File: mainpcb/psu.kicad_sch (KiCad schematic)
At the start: 15 parts, among them U1 LM22678TJ-5, U2 LM2576T-3.3

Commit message: Added PSU terminal block symbol
Also created bh_part_library for custom modelled parts used in the bot-hoven project.
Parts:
- added J1: 8PCV-06-006, symbol bh_part_library:8PCV-06-006
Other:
- note added: "SCREW TERMINALS TO MEANWELL LRS-XXX-24 POWER SUPPLY XXX - POWER RATING NOT YET SPECIFIED (200-350W)"
- moved on the sheet: C1, C2, C3, C4, C5, C6, C7, C8, C9, D1, D2, L1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

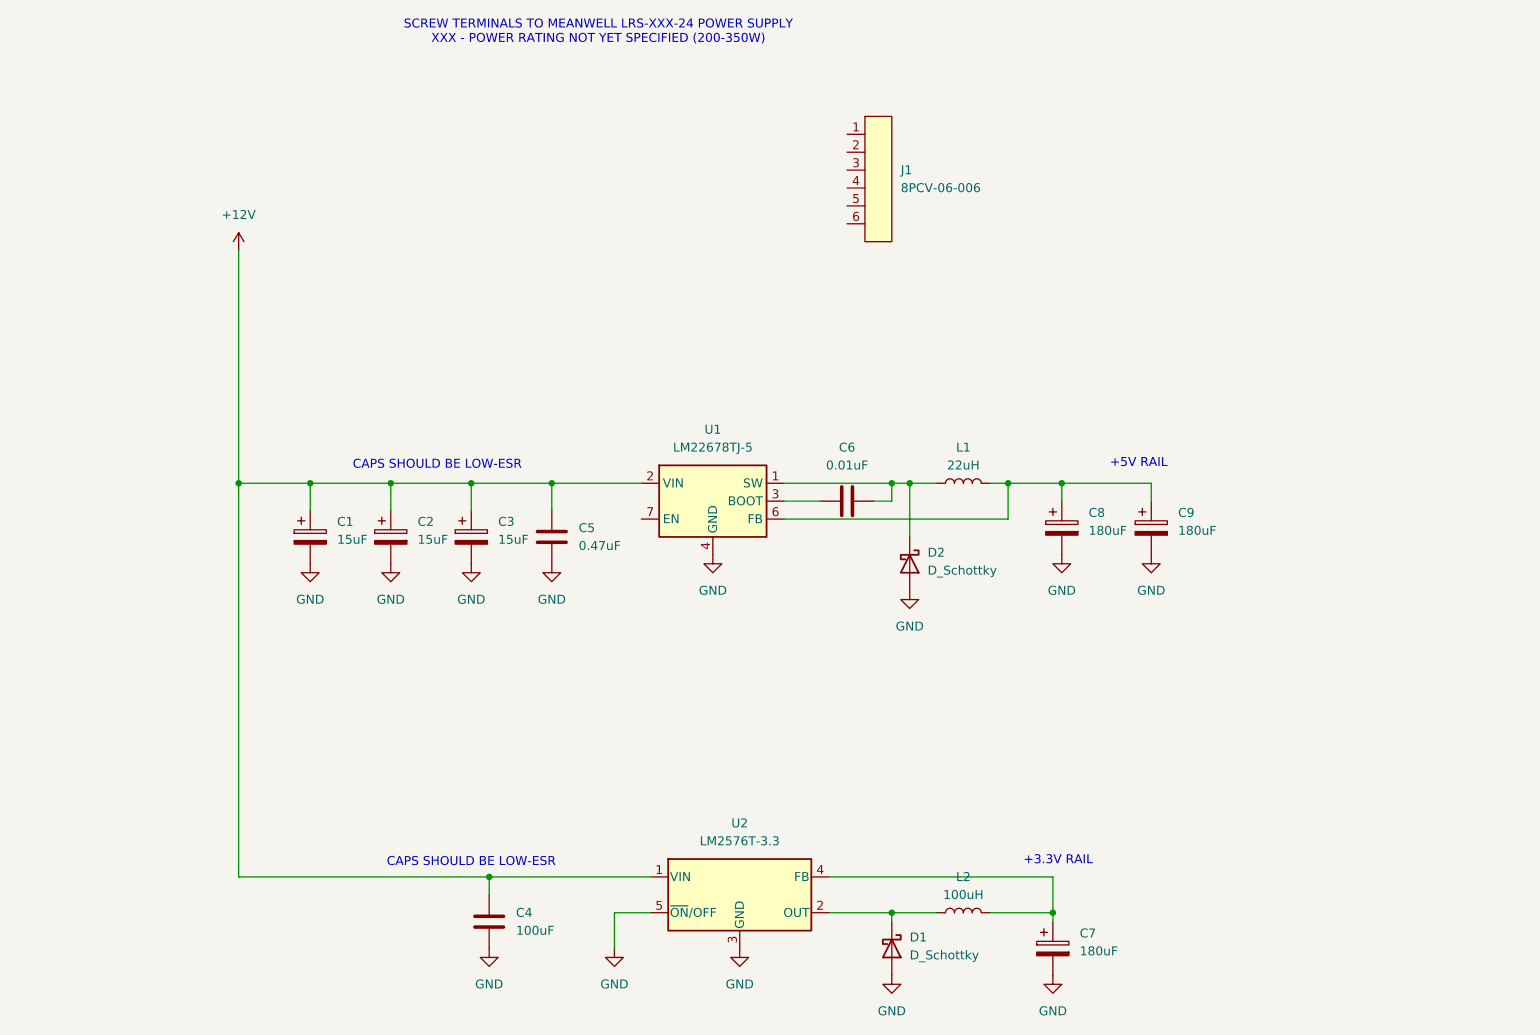
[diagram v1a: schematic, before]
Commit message: Some hand components, PSU changes
Updated PSU to 24V rail regulated to 5V and 3.3V. Hopefully we won't need a 12V rail. Made some part selections, added IO expander for hand, mosfet, made solenoid symbol.
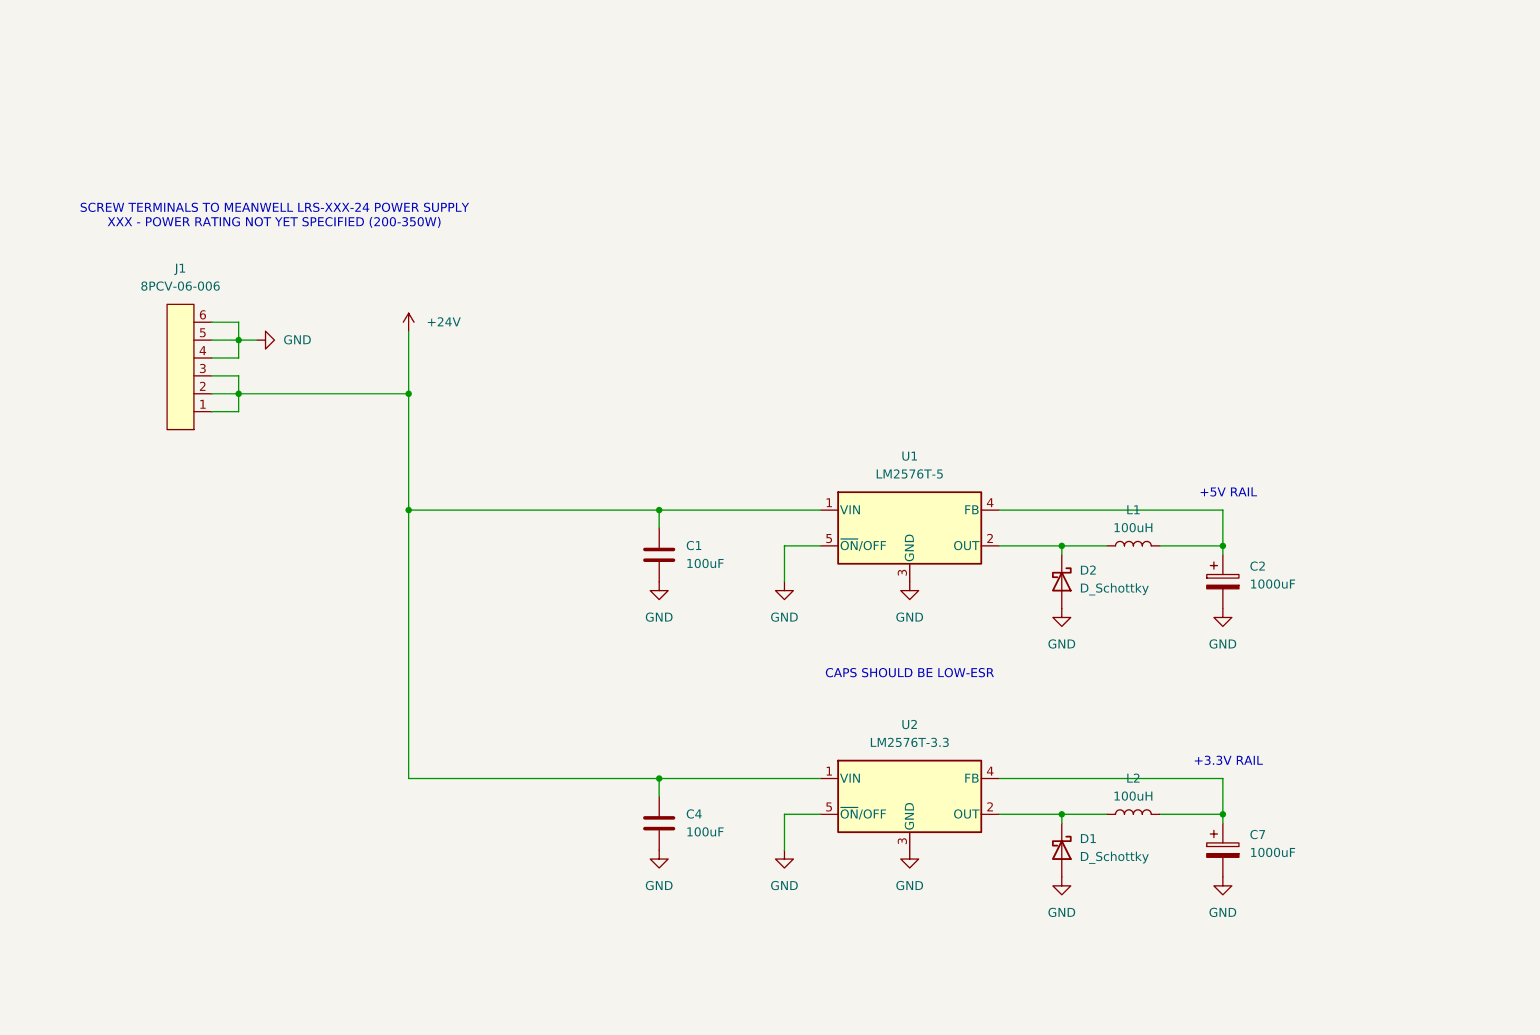
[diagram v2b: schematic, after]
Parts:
- removed C1, C3: 15uF, symbol Device:C_Polarized
- removed C5: 0.47uF, symbol Device:C
- removed C6: 0.01uF, symbol Device:C
- removed C8, C9: 180uF, symbol Device:C_Polarized
- removed J1: 8PCV-06-006, symbol bh_part_library:8PCV-06-006
- removed U1: LM22678TJ-5, Package_TO_SOT_THT:TO-220-7_P2.54x3.7mm_StaggerOdd_Lead3.8mm_Vertical, symbol Regulator_Switching:LM22678TJ-5
- added C1: 100uF, symbol Device:C
- added J1: 8PCV-06-006, symbol bh_symbol_library:8PCV-06-006
- added U1: LM2576T-5, Package_TO_SOT_THT:TO-220-5_Vertical, symbol Regulator_Switching:LM2576T-5
- C2: value 15uF -> 1000uF
- C7: value 180uF -> 1000uF
- L1: value 22uH -> 100uH
- U2: footprint Package_TO_SOT_THT:TO-220-5_Vertical -> Package_TO_SOT_THT:TO-220-5_P3.4x3.7mm_StaggerOdd_Lead3.8mm_Vertical; Digikey (none) -> https://www.digikey.ca/en/products/detail/texas-instruments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
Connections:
- net GND: now also C1.2, J1.4, J1.5, J1.6, U1.3 (GND), U1.5 (~{ON}/OFF)
- net at D2.1 (K), L1.1: now also U1.2 (OUT)
- net at L1.2: now also C2.1, U1.4 (FB)
- net +12V renamed +24V
- net +24V: now also C1.1, J1.1, J1.2, J1.3, U1.1 (VIN); no longer C2.1
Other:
- moved on the sheet: C4, C7, D1, L2, U2

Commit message: Added 12V power rail and regulator
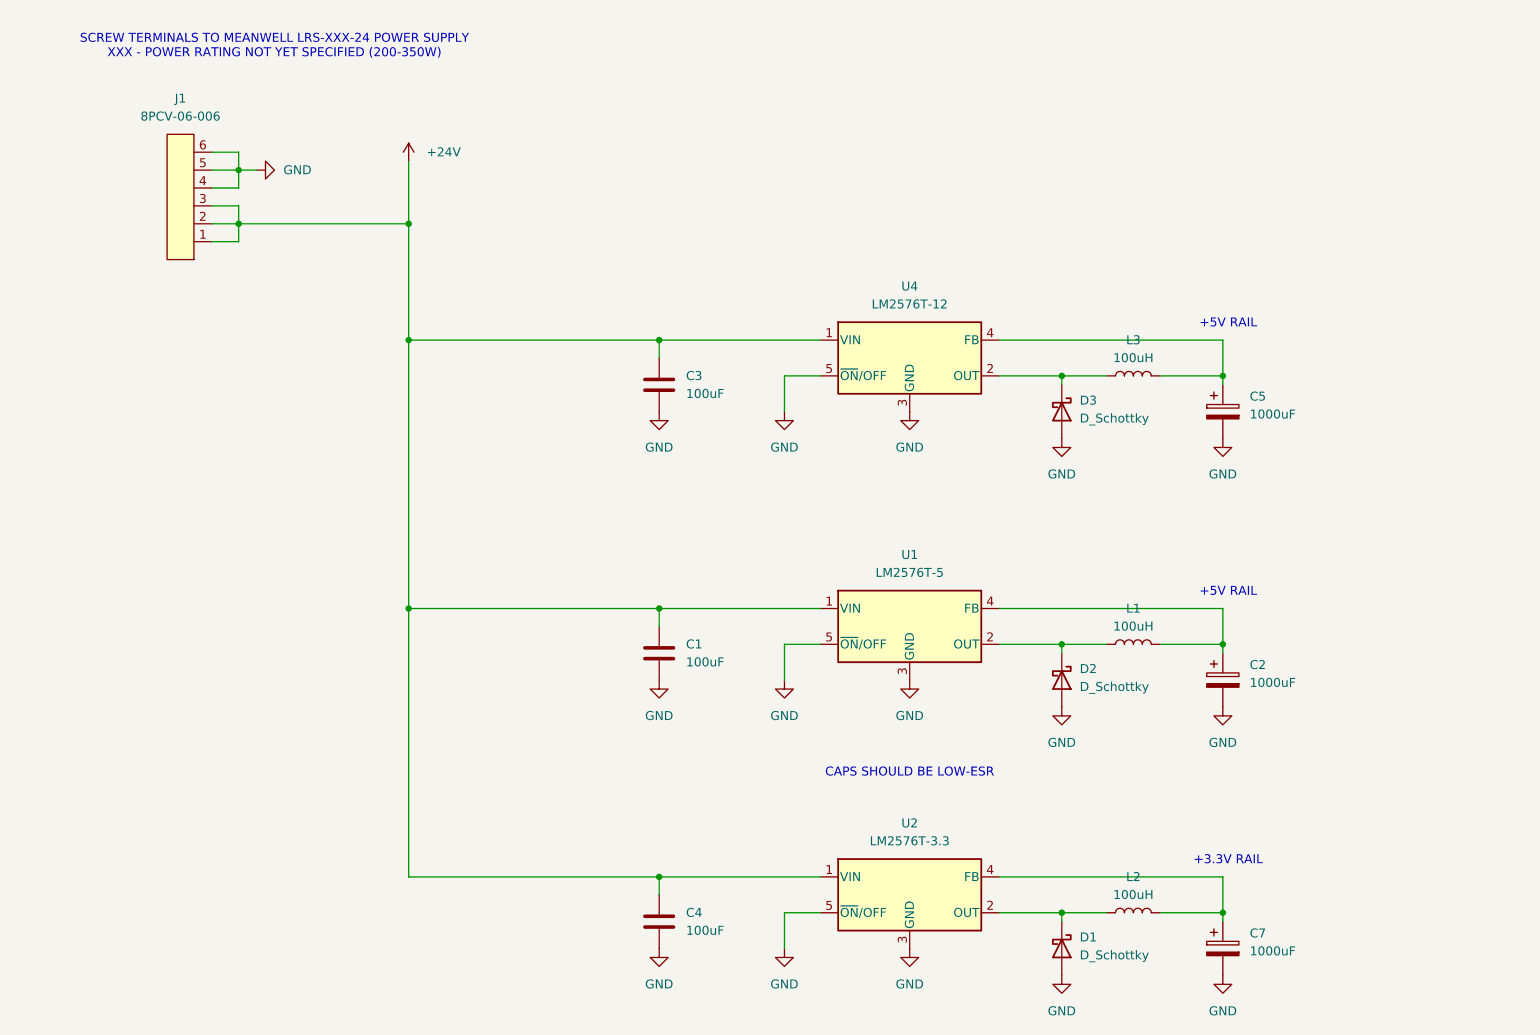
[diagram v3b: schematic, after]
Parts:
- added C3: 100uF, symbol Device:C
- added C5: 1000uF, symbol Device:C_Polarized
- added D3: D_Schottky, symbol Device:D_Schottky
- added L3: 100uH, symbol Device:L
- added U4: LM2576T-12, Package_TO_SOT_THT:TO-220-5_Vertical, symbol Regulator_Switching:LM2576T-12
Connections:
- net +24V: now also C3.1, U4.1 (VIN)
- net GND: now also C3.2, C5.2, D3.2 (A), U4.3 (GND), U4.5 (~{ON}/OFF)
- new net: D3.1 (K), L3.1, U4.2 (OUT)
- new net: C5.1, L3.2, U4.4 (FB)
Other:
- moved on the sheet: C1, C2, C4, C7, D1, D2, J1, L1, L2, U1, U2

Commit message: Created LM2678 12V regulator symbol
Updated 12V regulator circuit
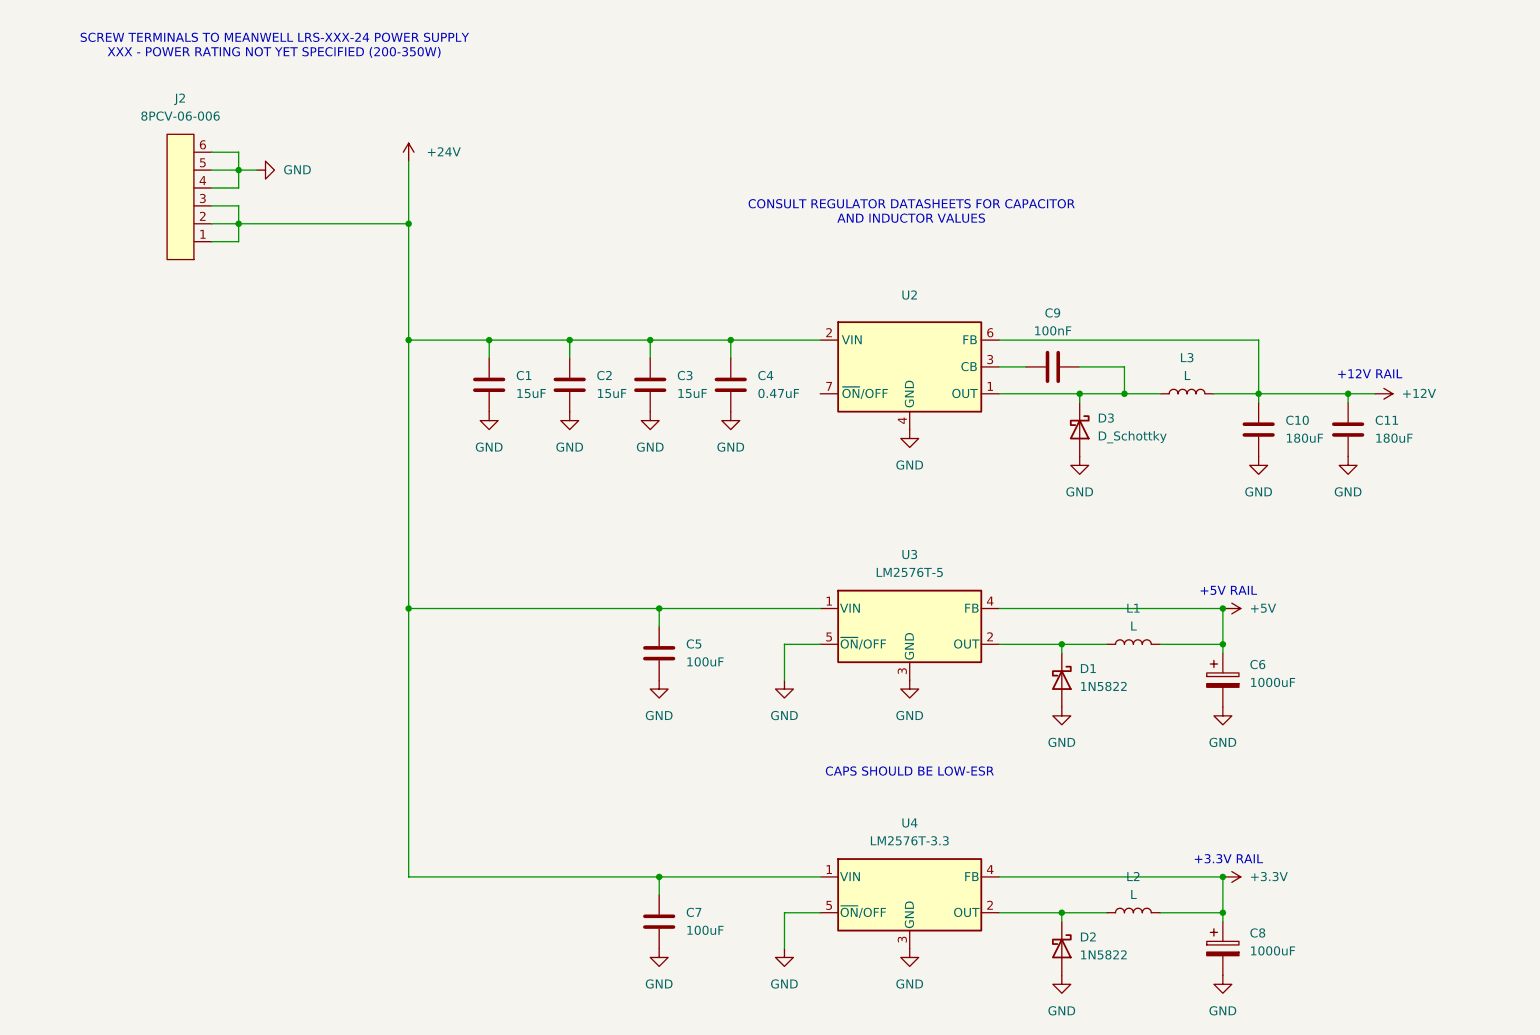
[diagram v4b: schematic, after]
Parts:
- removed C5: 1000uF, symbol Device:C_Polarized
- removed U4: LM2576T-12, Package_TO_SOT_THT:TO-220-5_Vertical, symbol Regulator_Switching:LM2576T-12
- added C1, C2: 15uF, symbol Device:C
- added C10, C11: 180uF, symbol Device:C
- added C4: 0.47uF, symbol Device:C
- added C9: 100nF, symbol Device:C
- added U2: ~, symbol bh_symbol_library:LM2678T-12
- C3: value 100uF -> 15uF
- D1: renamed from D2; value D_Schottky -> 1N5822
- D2: renamed from D1; value D_Schottky -> 1N5822
- D3: footprint (none) -> Package_TO_SOT_SMD:TO-263-2
- L1, L2, L3: value 100uH -> L
- renumbered C1 to C5, C2 to C6, C4 to C7, C7 to C8, J1 to J2, U1 to U3, U2 to U4
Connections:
- net +24V: now also C1.1, C2.1, C4.1, U2.2 (VIN)
- net GND: now also C1.2, C10.2, C11.2, C2.2, C4.2, U2.4 (GND)
- net at D3.1 (K), L3.1: now also C9.2, U2.1 (OUT)
- net +12V: now reaches L3.2
- net +12V: now also C10.1, C11.1, U2.6 (FB)
- net +3.3V: now reaches C8.1, L2.2, U4.4 (FB)
- net +5V: now reaches C6.1, L1.2, U3.4 (FB)
- new net: C9.1, U2.3 (CB)
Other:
- note added: "+12V RAIL"
- note added: "CONSULT REGULATOR DATASHEETS FOR CAPACITOR AND INDUCTOR VALUES"

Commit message: I2C transceivers, sheet hierarchy changes
Added I2C transceivers for both hands on the controller side, also changed sheet hierarchy to modularize controller board sheet somewhat
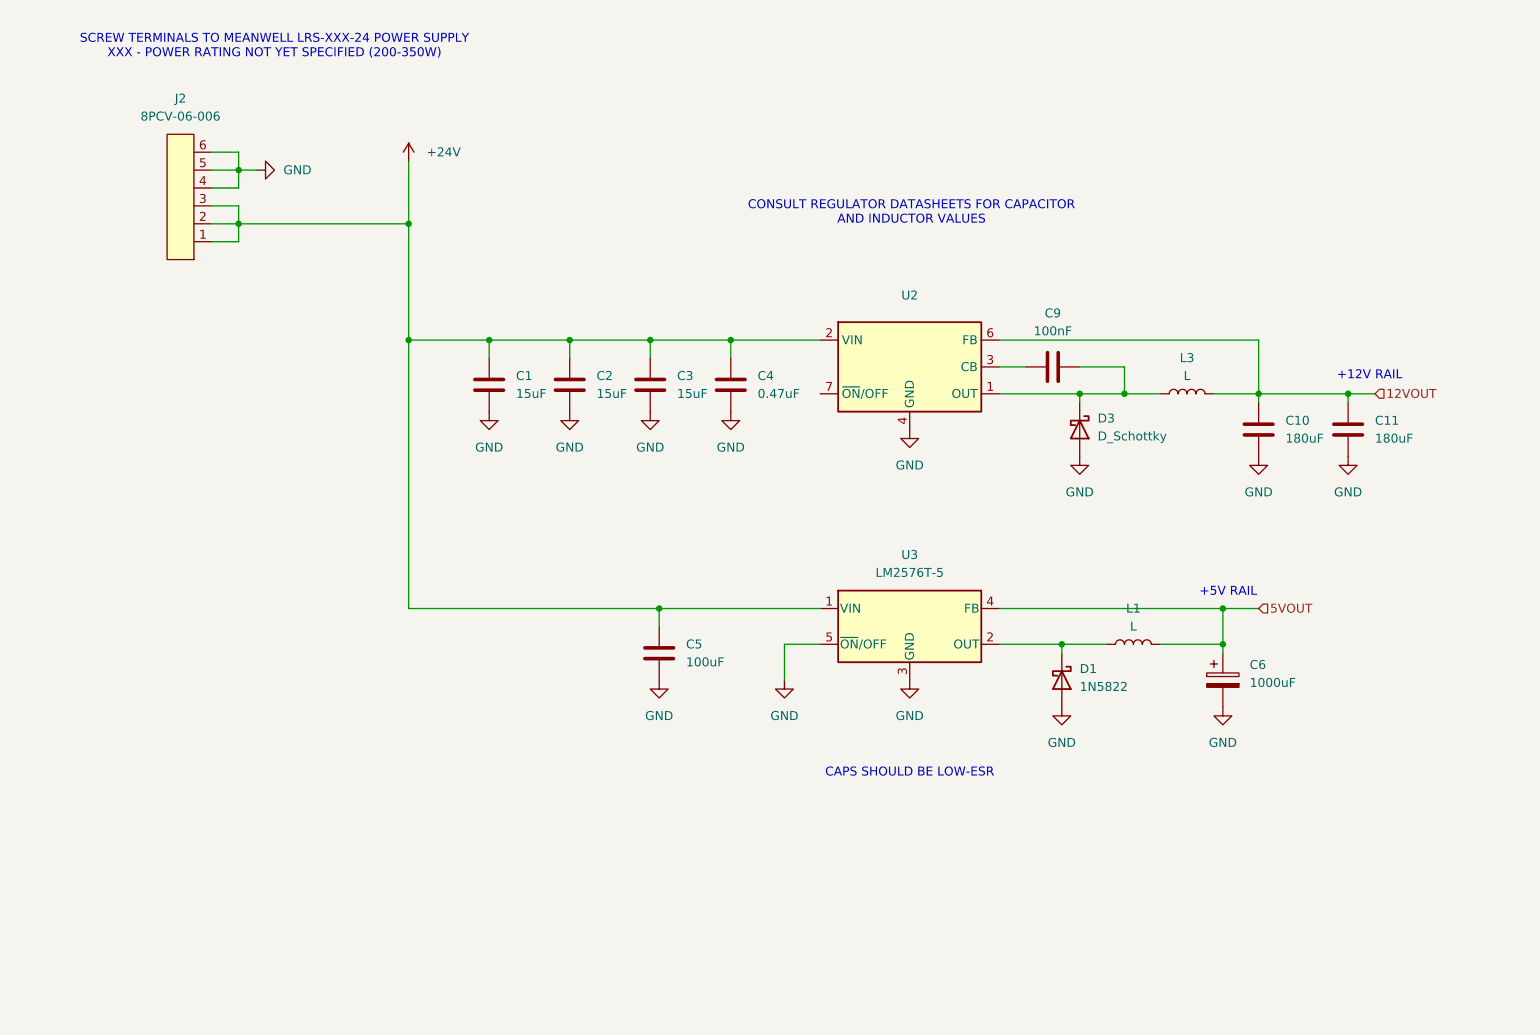
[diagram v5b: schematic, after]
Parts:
- removed C7: 100uF, symbol Device:C
- removed C8: 1000uF, symbol Device:C_Polarized
- removed D2: 1N5822, symbol Device:D_Schottky
- removed L2: L, symbol Device:L
- removed U4: LM2576T-3.3, Package_TO_SOT_THT:TO-220-5_P3.4x3.7mm_StaggerOdd_Lead3.8mm_Vertical, symbol Regulator_Switching:LM2576T-3.3
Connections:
- net +12V renamed 12VOUT
- net +5V renamed 5VOUT
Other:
- note removed: "+3.3V RAIL"

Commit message: Added current and voltage sensing on control board
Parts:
- U3: footprint Package_TO_SOT_THT:TO-220-5_Vertical -> Package_TO_SOT_THT:TO-220-5_P3.4x3.7mm_StaggerOdd_Lead3.8mm_Vertical
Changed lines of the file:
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@@
 			)
 		)
-		(property "Footprint" "Package_TO_SOT_THT:TO-220-5_Vertical"
+		(property "Footprint" "Package_TO_SOT_THT:TO-220-5_P3.4x3.7mm_StaggerOdd_Lead3.8mm_Vertical"
 			(at 166.37 110.49 0)
 			(effects
